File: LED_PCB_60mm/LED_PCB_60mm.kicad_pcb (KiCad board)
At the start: 2 copper layers, 60 x 60 mm, 9 parts, among them J1 Conn_01x01_Female, J2 Conn_01x01_Female, J3 Conn_01x01_Female, J4 Conn_01x01_Female, J5 Conn_01x01_Female, J6 Conn_01x01_Female

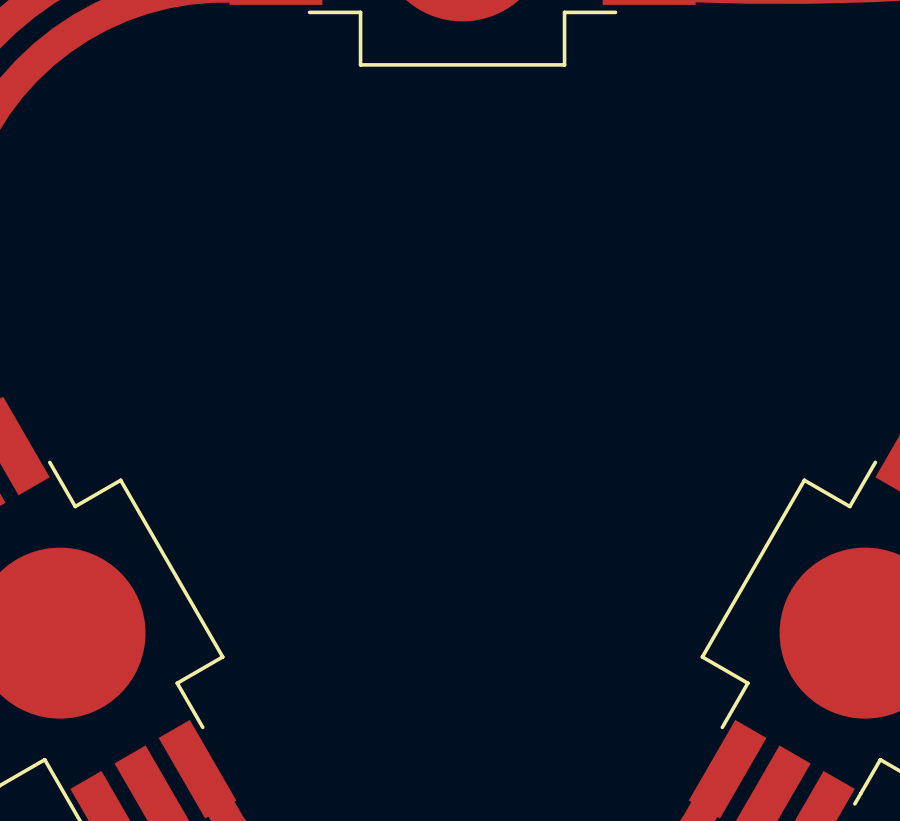
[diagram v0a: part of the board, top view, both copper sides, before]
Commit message: generate LED fabrication files
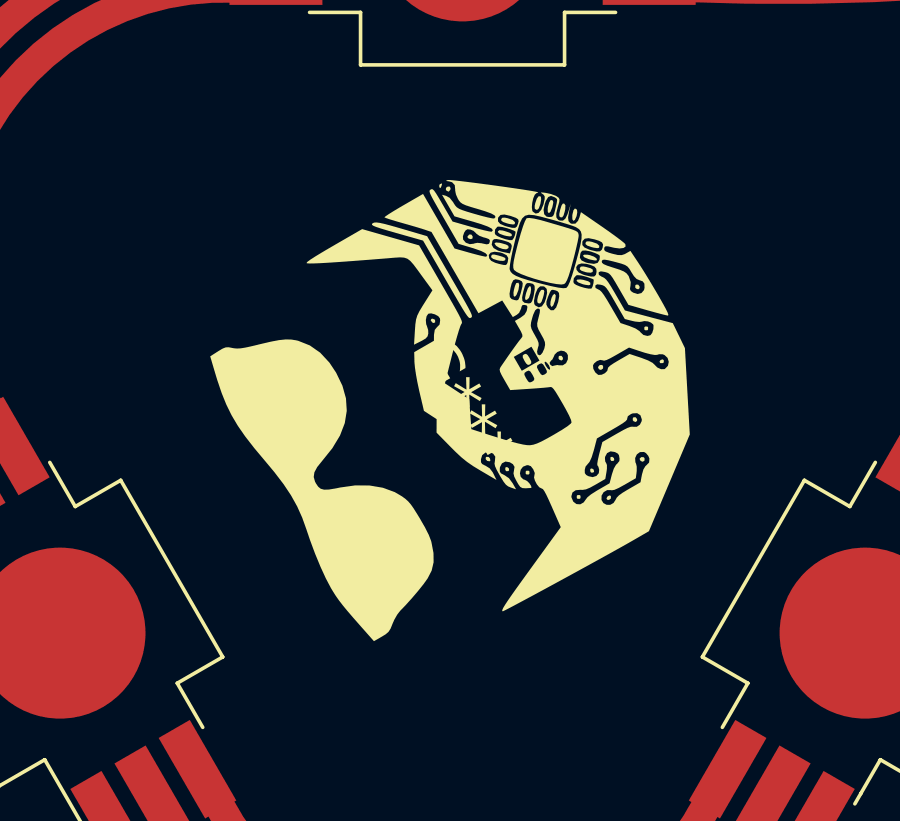
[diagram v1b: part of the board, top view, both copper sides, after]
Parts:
- added G***: LOGO, LOGO, F.Cu at (150.2, 90.3)

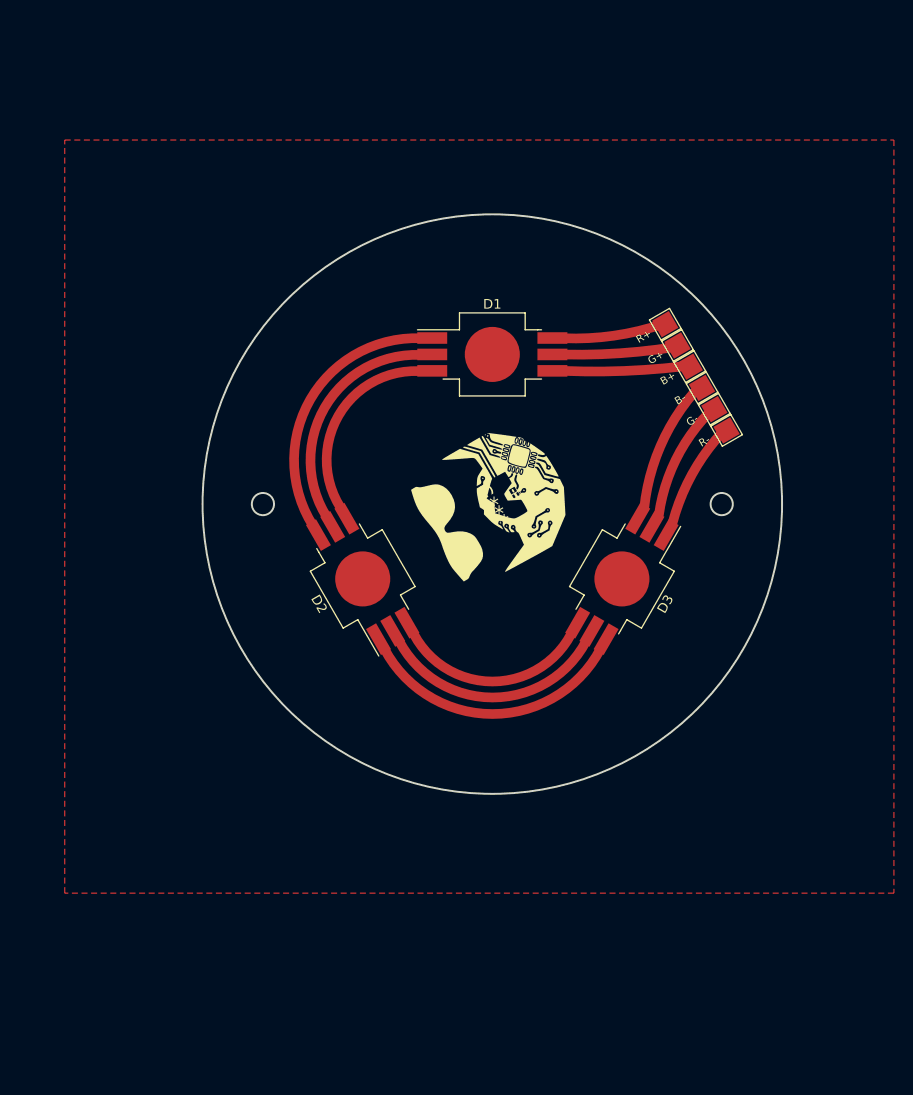
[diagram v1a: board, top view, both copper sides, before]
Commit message: Aufteilen der 3 Heatpads
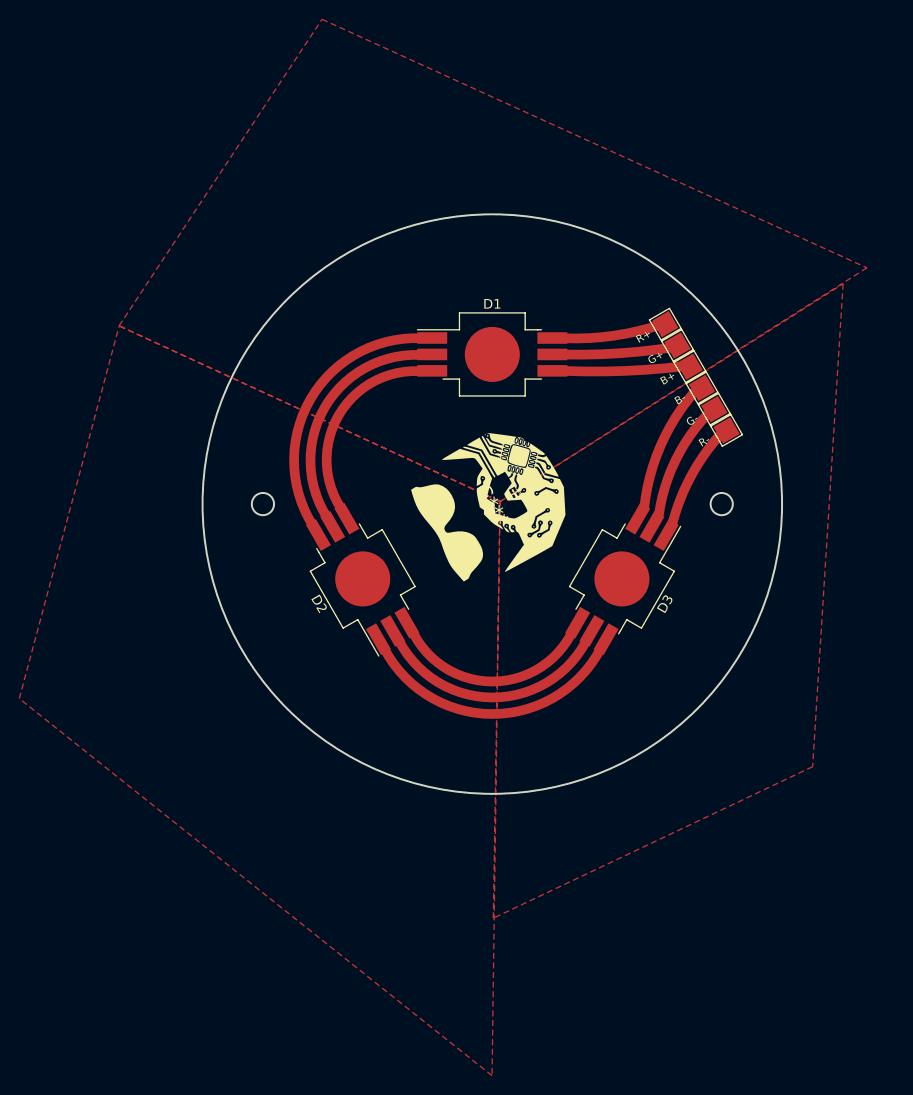
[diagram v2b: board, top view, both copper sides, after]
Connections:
- D1 pad PAD: GND -> GND1
- D2 pad PAD: GND -> GND2
- D3 pad PAD: GND -> GND3
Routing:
- added copper zone on F.Cu, net GND1
- added copper zone on F.Cu, net GND2
- added copper zone on F.Cu, net GND3
- removed copper zone on F.Cu, net GND
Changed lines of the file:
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@@
   (net 11 "Net-(D3-Pad2)")
   (net 12 "Net-(D3-Pad3)")
-  (net 13 "GND")
+  (net 13 "GND1")
+  (net 14 "GND2")
+  (net 15 "GND3")
   (footprint "TestPoint:TestPoint_Pad_2.0x2.0mm" (layer "F.Cu")
     (at 173.228 80.345409 -60)
@@
       (net 3 "Net-(D1-Pad6)") (pinfunction "RA") (pintype "passive"))
     (pad "PAD" smd circle (at 0 0) (size 5.7 5.7) (layers "F.Cu" "F.Paste" "F.Mask")
-      (net 13 "GND"))
+      (net 13 "GND1"))
     (model "${KICAD6_3DMODEL_DIR}/LED_SMD.3dshapes/LED_RGB_Getian_GT-P6PRGB4303.wrl"
       (offset (xyz 0 0 0))
@@
       (net 7 "Net-(D2-Pad1)") (pinfunction "RA") (pintype "passive"))
     (pad "PAD" smd circle (at 0 0 240) (size 5.7 5.7) (layers "F.Cu" "F.Paste" "F.Mask")
-      (net 13 "GND"))
+      (net 15 "GND3"))
     (model "${KICAD6_3DMODEL_DIR}/LED_SMD.3dshapes/LED_RGB_Getian_GT-P6PRGB4303.wrl"
       (offset (xyz 0 0 0))
@@
       (net 4 "Net-(D1-Pad1)") (pinfunction "RA") (pintype "passive"))
     (pad "PAD" smd circle (at 0 0 120) (size 5.7 5.7) (layers "F.Cu" "F.Paste" "F.Mask")
-      (net 13 "GND"))
+      (net 14 "GND2"))
     (model "${KICAD6_3DMODEL_DIR}/LED_SMD.3dshapes/LED_RGB_Getian_GT-P6PRGB4303.wrl"
       (offset (xyz 0 0 0))
@@
   (segment (start 144.022 76.45) (end 144.018 76.454) (width 0.25) (layer "F.Cu") (net 6))
   (segment (start 144.022 76.376) (end 144.022 76.45) (width 0.25) (layer "F.Cu") (net 6))
-  (zone (net 13) (net_name "GND") (layer "F.Cu") (hatch edge 0.508)
+  (zone (net 14) (net_name "GND2") (layer "F.Cu") (hatch edge 0.508)
+    (priority 2)
     (connect_pads yes (clearance 0.508))
     (min_thickness 0.254) (filled_areas_thickness no)
@@
     (polygon
       (pts
-        (xy 191.8208 130.4544)
-        (xy 105.9688 130.4544)
-        (xy 105.9688 52.4764)
-        (xy 191.8208 52.4764)      )
+        (xy 101.270316 110.307336)
+        (xy 111.6076 71.7296)
+        (xy 151.0284 89.916)
+        (xy 150.2156 149.352)      )
     )
   )
+  (zone (net 13) (net_name "GND1") (layer "F.Cu") (hatch edge 0.508)
+    (connect_pads yes (clearance 0.508))
+    (min_thickness 0.254) (filled_areas_thickness no)
+    (fill yes (thermal_gap 0.508) (thermal_bridge_width 0.508))
+    (polygon
+      (pts
+        (xy 151.0538 89.8906)
+        (xy 111.6076 71.7042)
+        (xy 132.6134 39.9796)
+        (xy 189.0268 65.7098)      )
+    )
+  )
+  (zone (net 15) (net_name "GND3") (layer "F.Cu") (hatch edge 0.508)
+    (priority 1)
+    (connect_pads yes (clearance 0.508))
+    (min_thickness 0.254) (filled_areas_thickness no)
+    (fill yes (thermal_gap 0.508) (thermal_bridge_width 0.508))
+    (polygon
+      (pts
+        (xy 183.405134 117.361407)
+        (xy 150.3426 133.0452)
+        (xy 151.0538 89.916)
+        (xy 186.563 67.3608)      )
+    )
+  )
